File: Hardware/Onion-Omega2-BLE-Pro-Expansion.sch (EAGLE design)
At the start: 37 parts, among them J1 USB-MICROB, J2 USB-A-H, U2 ONION-OMEGA2

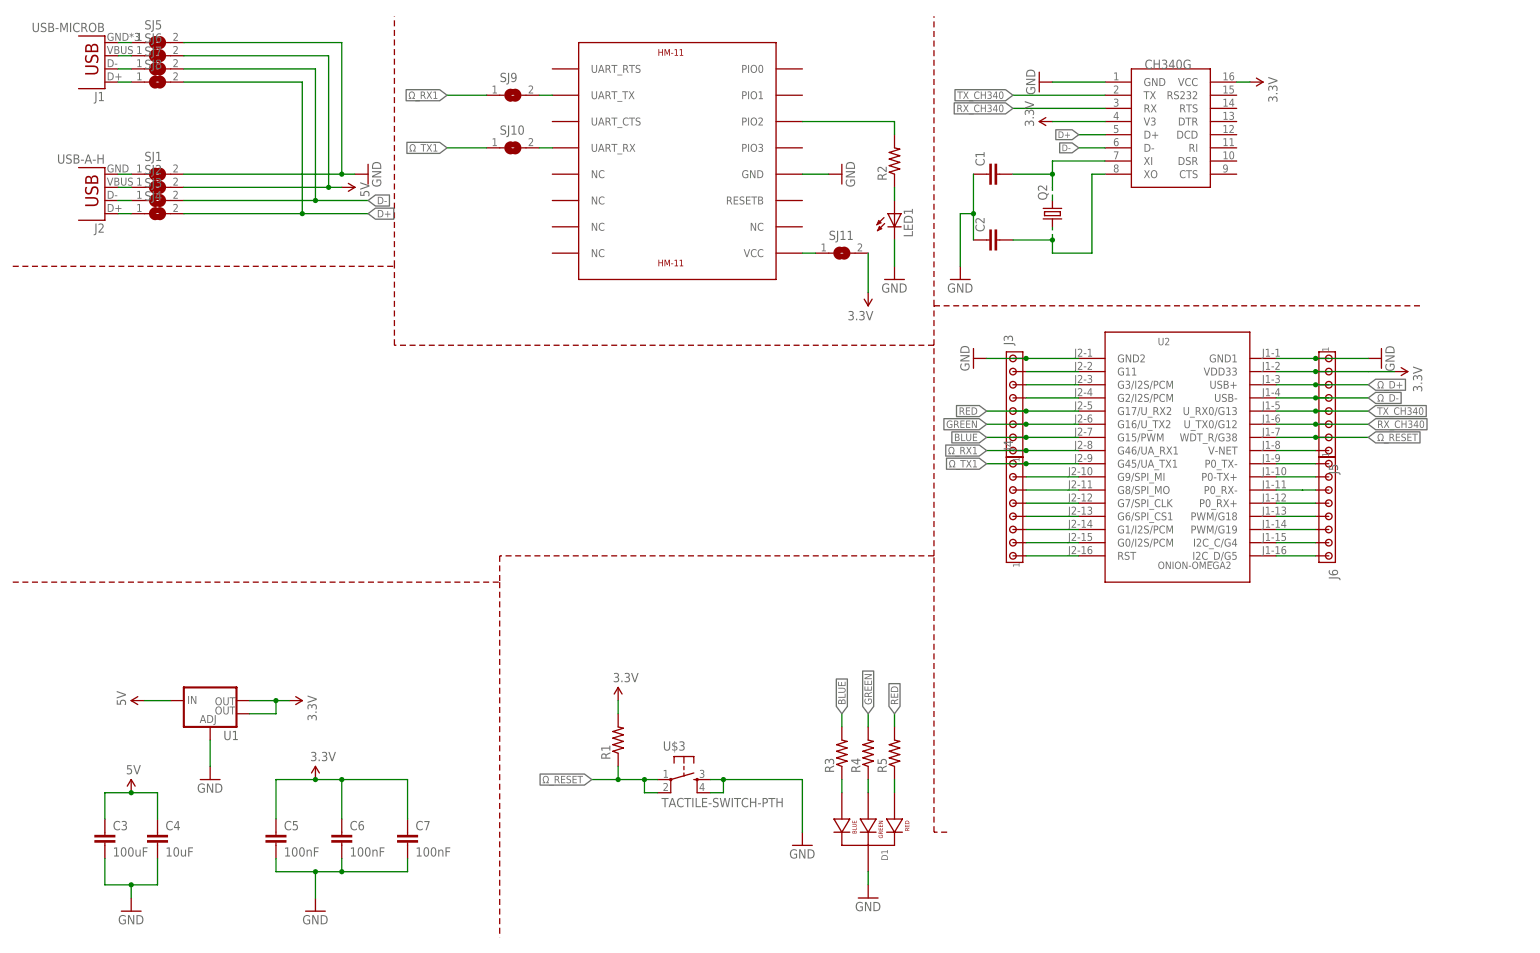
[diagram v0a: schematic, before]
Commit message: Board Size reduced. Replaced almost all PTH with SMD. CH340G breakout. Minor improvements. Halfway manual routing. Lots of DRC errors
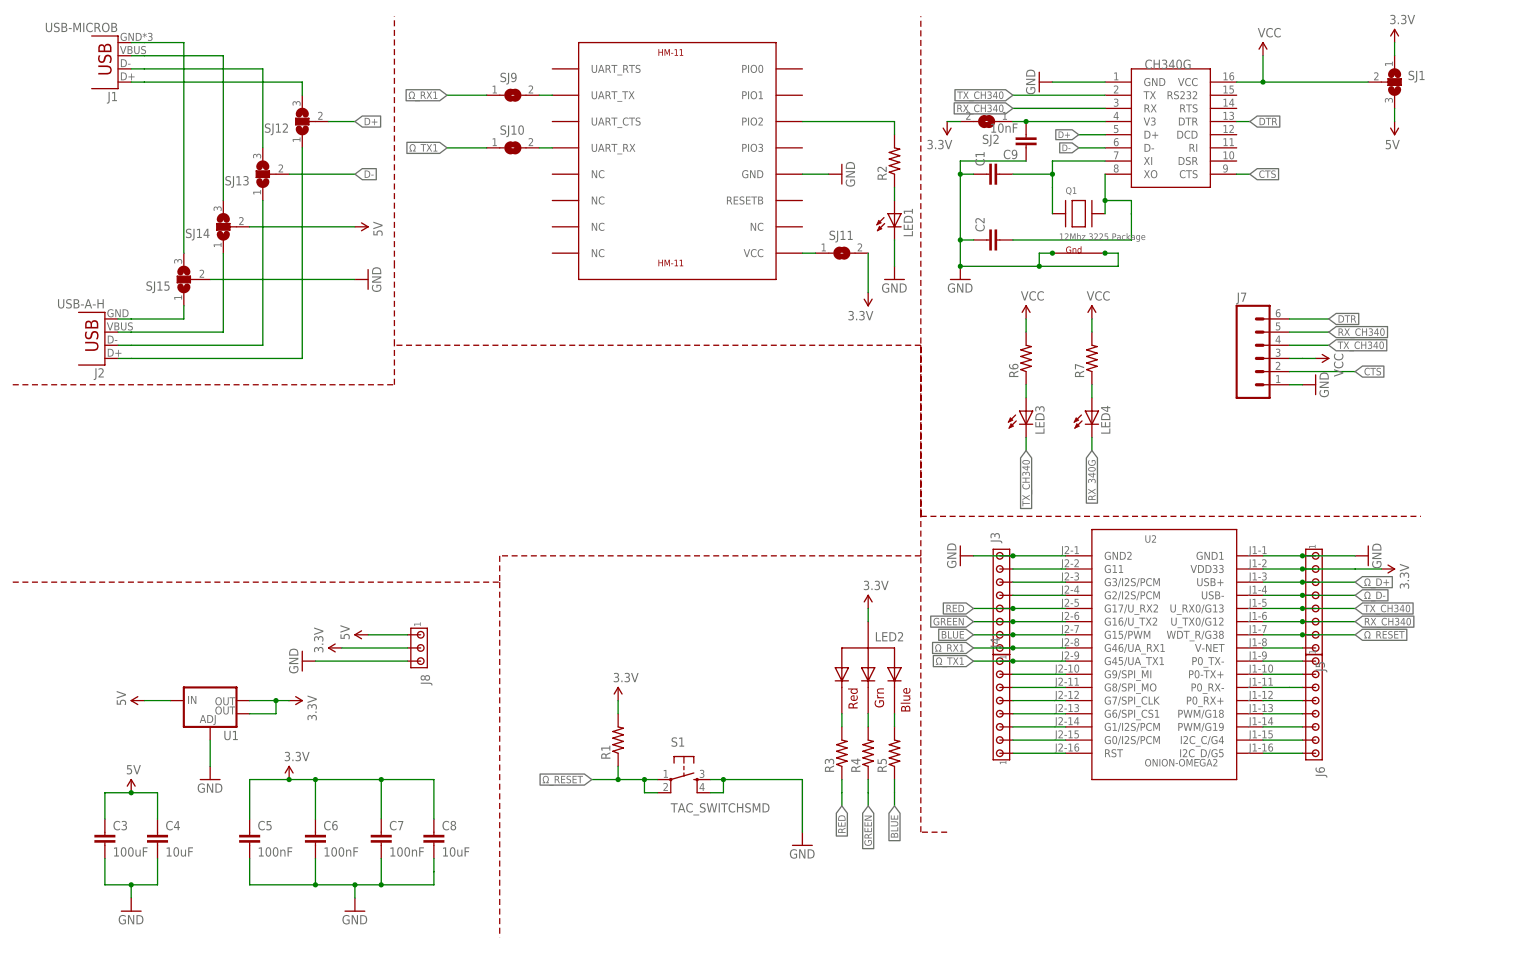
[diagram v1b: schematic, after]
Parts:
- removed D1: LED-RGB-CC-THRUCLEAR, SparkFun-LED:LED-RGB-CC-THRUCLEAR
- removed Q2: (no value), adafruit:CRYSTALHC49U-V
- removed SJ3, SJ4, SJ5, SJ6, SJ7, SJ8: (no value), jumper:SJ
- removed U$3: TACTILE-SWITCH-PTH, GeekAmmo:TACTILE-SWITCH-PTH
- added C8: 10uF, SparkFun-Passives:CAP1206
- added C9: 10nF, SparkFun-Passives:CAP1206
- added J7: (no value), SparkFun-Connectors:M06SMD-FEMALE-V2
- added J8: (no value), con-amp:MTA03-100
- added LED2: RGBLED_CA-PIRANHA, adafruit:RGBLED_CA-PIRANHA
- added LED3, LED4: (no value), adafruit:LEDCHIPLED_1206
- added Q1: 12Mhz 3225 Package, adafruit:XTAL-4-3225
- added R6, R7: (no value), SparkFun-Passives:RESISTOR1206
- added S1: TAC_SWITCHSMD, SparkFun-Retired:TAC_SWITCHSMD
- added SJ12, SJ13, SJ14, SJ15: (no value), jumper:SJ2W
- C1, C2, C3, C4, C5, C6, C7: device SparkFun-Capacitors:CAPKIT -> SparkFun-Passives:CAP1206
- LED1: device adafruit:LED3MM -> adafruit:LEDCHIPLED_1206
- R1, R2, R3, R4, R5: device adafruit:R-US_0204/7 -> SparkFun-Passives:RESISTOR1206
- SJ1: device jumper:SJ -> jumper:SJ2W
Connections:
- removed net N$10: D1.GREEN_CATHODE, R4.1
- new net CTS: J7.2, U$1.CTS
- new net DTR: J7.6, U$1.DTR
- new net N$21: LED2.RED, R3.2
- new net N$22: LED2.GREEN, R4.2
- new net N$23: LED2.BLUE, R5.2
- new net N$24: LED4.A, R7.1
- new net RX_340G: LED4.C
- new net VCC: J7.3, R6.2, R7.2, SJ1.2, U$1.VCC
- net 3.3V: now also C8.1, J8.2, LED2.VCC, SJ1.1, SJ2.2; no longer U$1.V3, U$1.VCC
- net 5V: now also J8.1, SJ1.3, SJ14.2; no longer SJ2.2, SJ6.2
- net BLUE: now also R5.1; no longer R3.2
- net D+: now also SJ12.2; no longer SJ4.2, SJ8.2
- net D-: now also SJ13.2; no longer SJ3.2, SJ7.2
- net GND: now also C8.2, C9.1, J7.1, J8.3, Q1.G1, Q1.G2, S1.3, S1.4, SJ15.2; no longer D1.CATHODE, SJ1.2, SJ5.2, U$3.3, U$3.4
- net GREEN: now also R4.1; no longer R4.2
- net N$1: now also Q1.X1; no longer Q2.2
- net N$11: now also LED3.A, R6.1; no longer D1.RED_CATHODE, R5.1
- net N$2: now also Q1.X2; no longer Q2.1
- net N$39: now also SJ15.1; no longer SJ1.1
- net N$40: now also SJ15.3; no longer SJ5.1
- net N$41: now also SJ14.3; no longer SJ6.1
- net N$42: now also SJ13.3; no longer SJ7.1
- net N$43: now also SJ12.3; no longer SJ8.1
- net N$44: now also SJ14.1; no longer SJ2.1
- net N$45: now also SJ13.1; no longer SJ3.1
- net N$46: now also SJ12.1; no longer SJ4.1
- net N$9: now also C9.2, SJ2.1, U$1.V3; no longer D1.BLUE_CATHODE, R3.1
- net RED: now also R3.1; no longer R5.2
- net RX_CH340: now also J7.5
- net TX_CH340: now also J7.4, LED3.C
- net Ω_RESET: now also S1.1, S1.2; no longer U$3.1, U$3.2
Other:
- moved on the sheet: C5, C6, C7, J1, J2, J3, J4, J5, J6, SJ2, U2

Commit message: Routing done with the help of autorouter. Not satisfied with few components placements
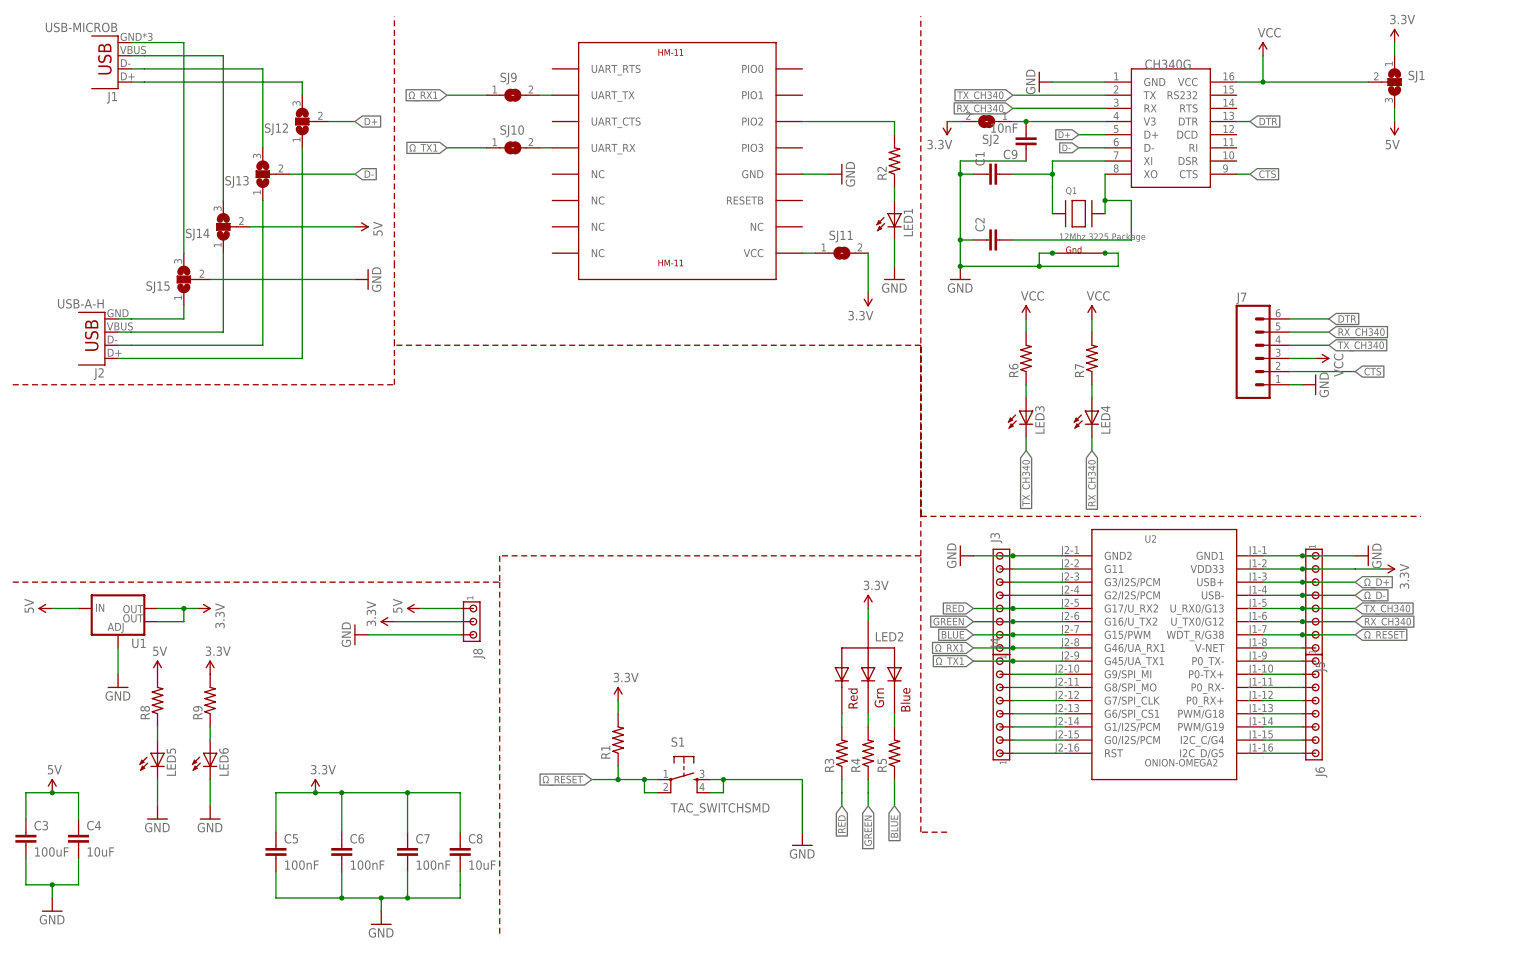
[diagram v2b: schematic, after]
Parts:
- added LED5, LED6: (no value), adafruit:LEDCHIPLED_1206
- added R8, R9: (no value), SparkFun-Passives:RESISTOR1206
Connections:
- removed net RX_340G: LED4.C
- new net N$25: LED5.A, R8.1
- new net N$26: LED6.A, R9.1
- net 3.3V: now also R9.2
- net 5V: now also R8.2
- net GND: now also LED5.C, LED6.C
- net RX_CH340: now also LED4.C
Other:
- moved on the sheet: C3, C4, C5, C6, C7, C8, J8, U1

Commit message: v0.1 freeze. Placements looks good.
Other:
- note added: "TODO: 1. SPI Port 2. I2C Port 3. Make the PCB Breadboard compatible"
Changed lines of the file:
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@@
 <wire x1="2.54" y1="109.22" x2="76.2" y2="109.22" width="0.1524" layer="94" style="dashdot"/>
 <wire x1="76.2" y1="109.22" x2="76.2" y2="116.84" width="0.1524" layer="94" style="dashdot"/>
+<text x="30.48" y="86.36" size="1.4224" layer="94">TODO:
+1. SPI Port
+2. I2C Port
+3. Make the PCB Breadboard compatible
+</text>
 </plain>
 <instances>
@@
 </schematic>
 </drawing>
+<compatibility>
+<note version="6.3" minversion="6.2.2" severity="warning">
+Since Version 6.2.2 text objects can contain more than one line,
+which will not be processed correctly with this version.
+</note>
+</compatibility>
 </eagle>

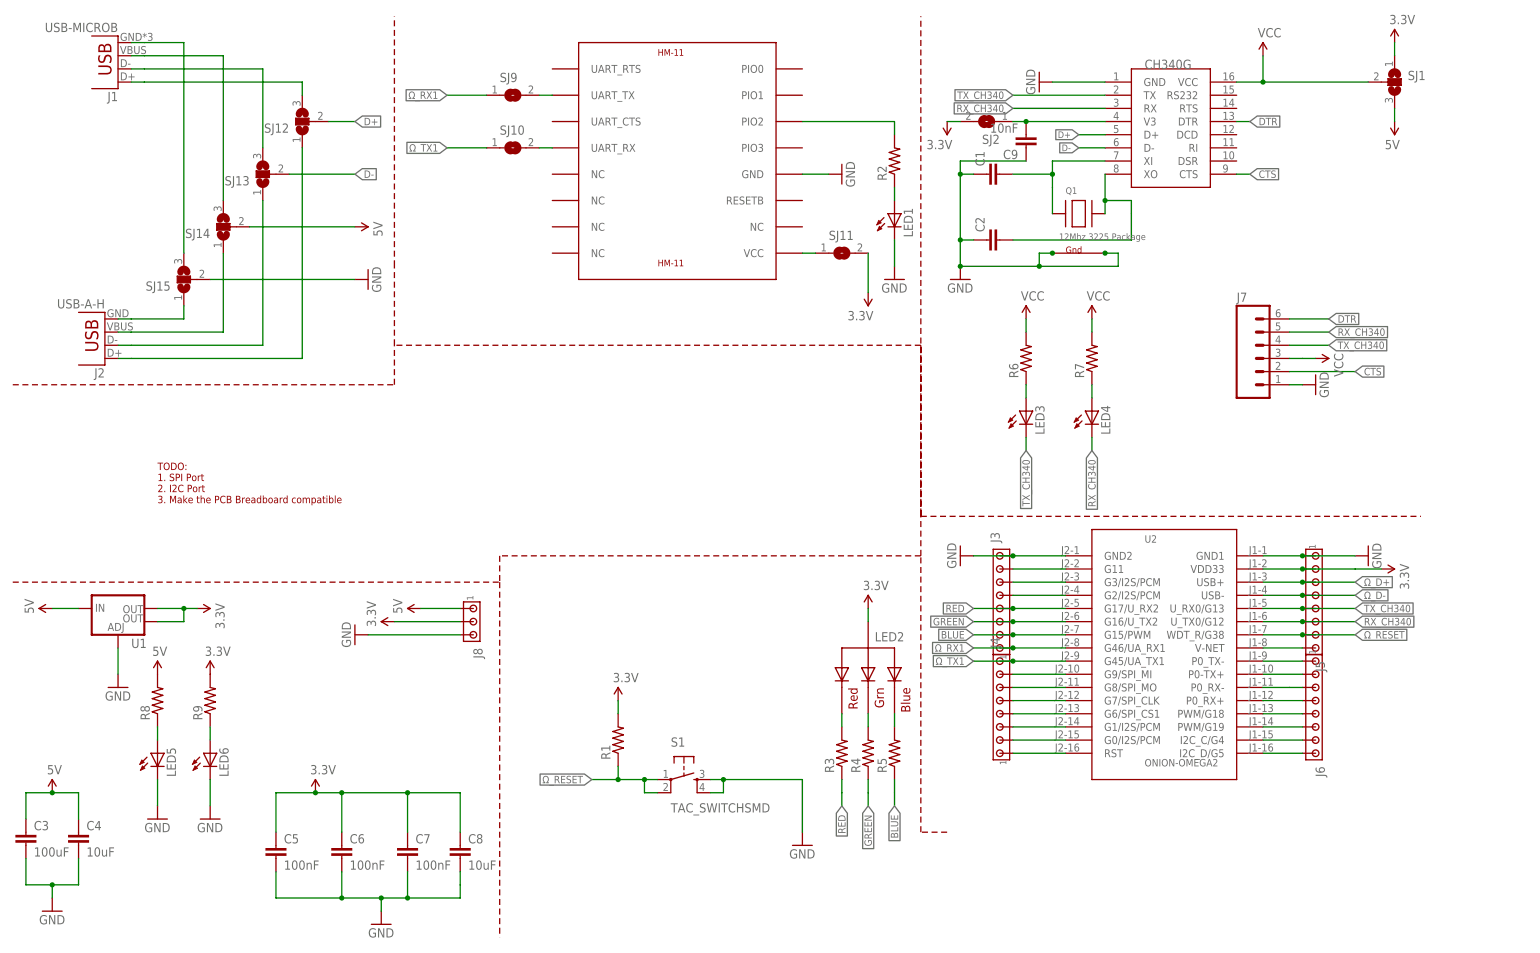
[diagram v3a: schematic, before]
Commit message: Silk Screen Fix
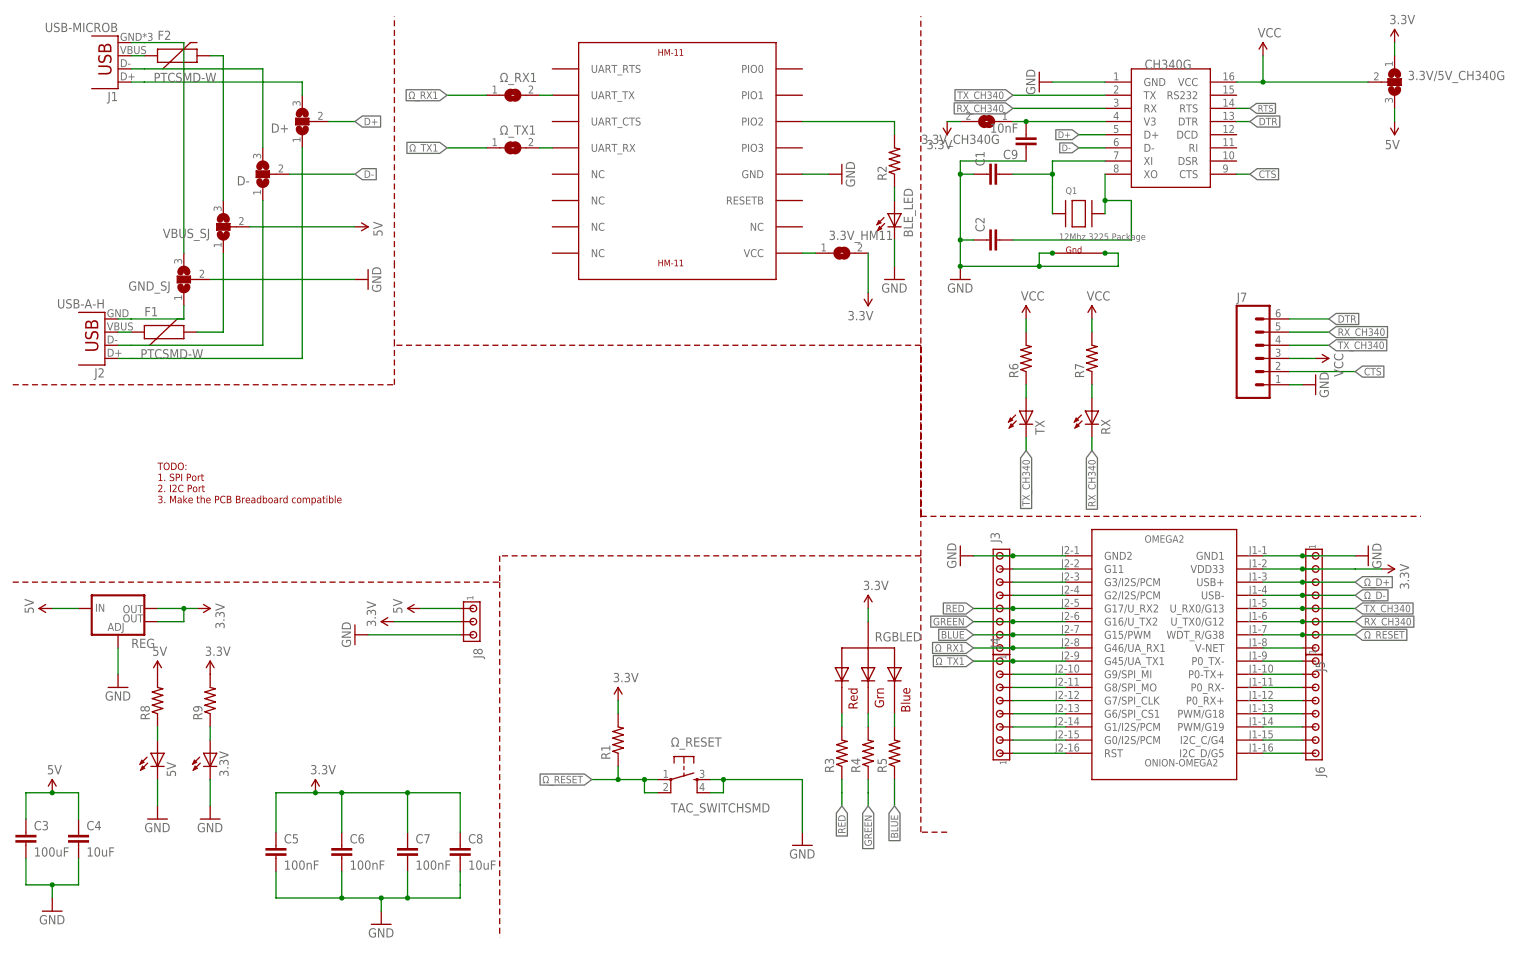
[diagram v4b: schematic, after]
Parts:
- added F1, F2: PTCSMD-W, SparkFun-PowerIC:PTCSMD-W
- renumbered LED1 to BLE_LED, LED2 to RGBLED, LED3 to TX, LED4 to RX, LED5 to 5V, LED6 to 3.3V, S1 to Ω_RESET, SJ1 to 3.3V/5V_CH340G, SJ10 to Ω_TX1, SJ11 to 3.3V_HM11, SJ12 to D+, SJ13 to D-, SJ14 to VBUS_SJ, SJ15 to GND_SJ, SJ2 to 3.3V_CH340G, SJ9 to Ω_RX1, U1 to REG, U2 to OMEGA2
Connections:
- new net N$27: F2.1, J1.VBUS
- new net N$37: F1.1, J2.VBUS
- new net RTS: U$1.RTS
- net N$41: now also F2.2; no longer J1.VBUS
- net N$44: now also F1.2; no longer J2.VBUS
